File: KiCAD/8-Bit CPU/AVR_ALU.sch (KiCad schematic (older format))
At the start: 23 parts, among them J2 AVRISP, U20 74HC377, U21 ATmega16-16AU, U22 74HC245, U23 74HC173

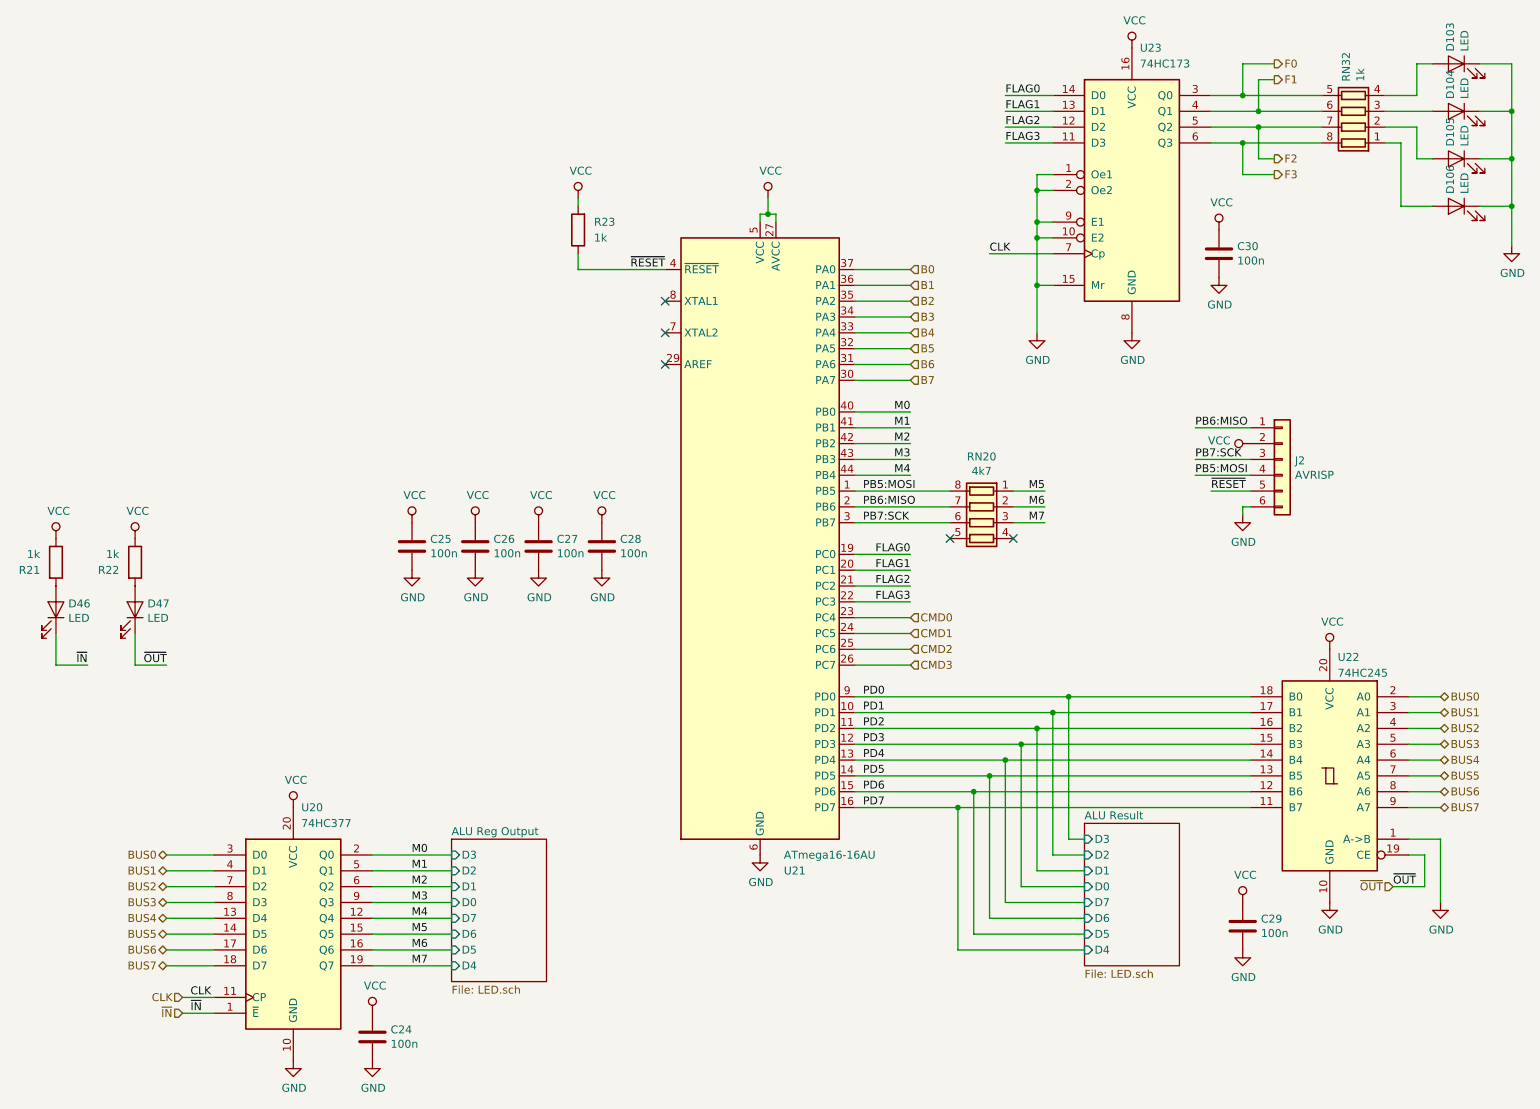
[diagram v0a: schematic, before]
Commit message: KiCAD cleanup - Revision A
Revision A Known Issues:
 * ATTiny45 has incorrect footprint
 * Flags register is redundant (The ATMega16's output port is a register)
 * Power jack pinout is wrong (12V shorted to ground)
 * Step counter reset logic is wrong (Active high signalling, Active low input)
 * ALU output indicator not connected
 * HLT indicator missing
 * EEPROMs can't be page written due to addressing setup (minor annoyance)
 * Flags Logic uses NAND gates instead of AND (fixed on the board I built)
 * Programmer needs to be able to toggle EEPROM outputs and Addressing Devices
    with different signals to enable reading.
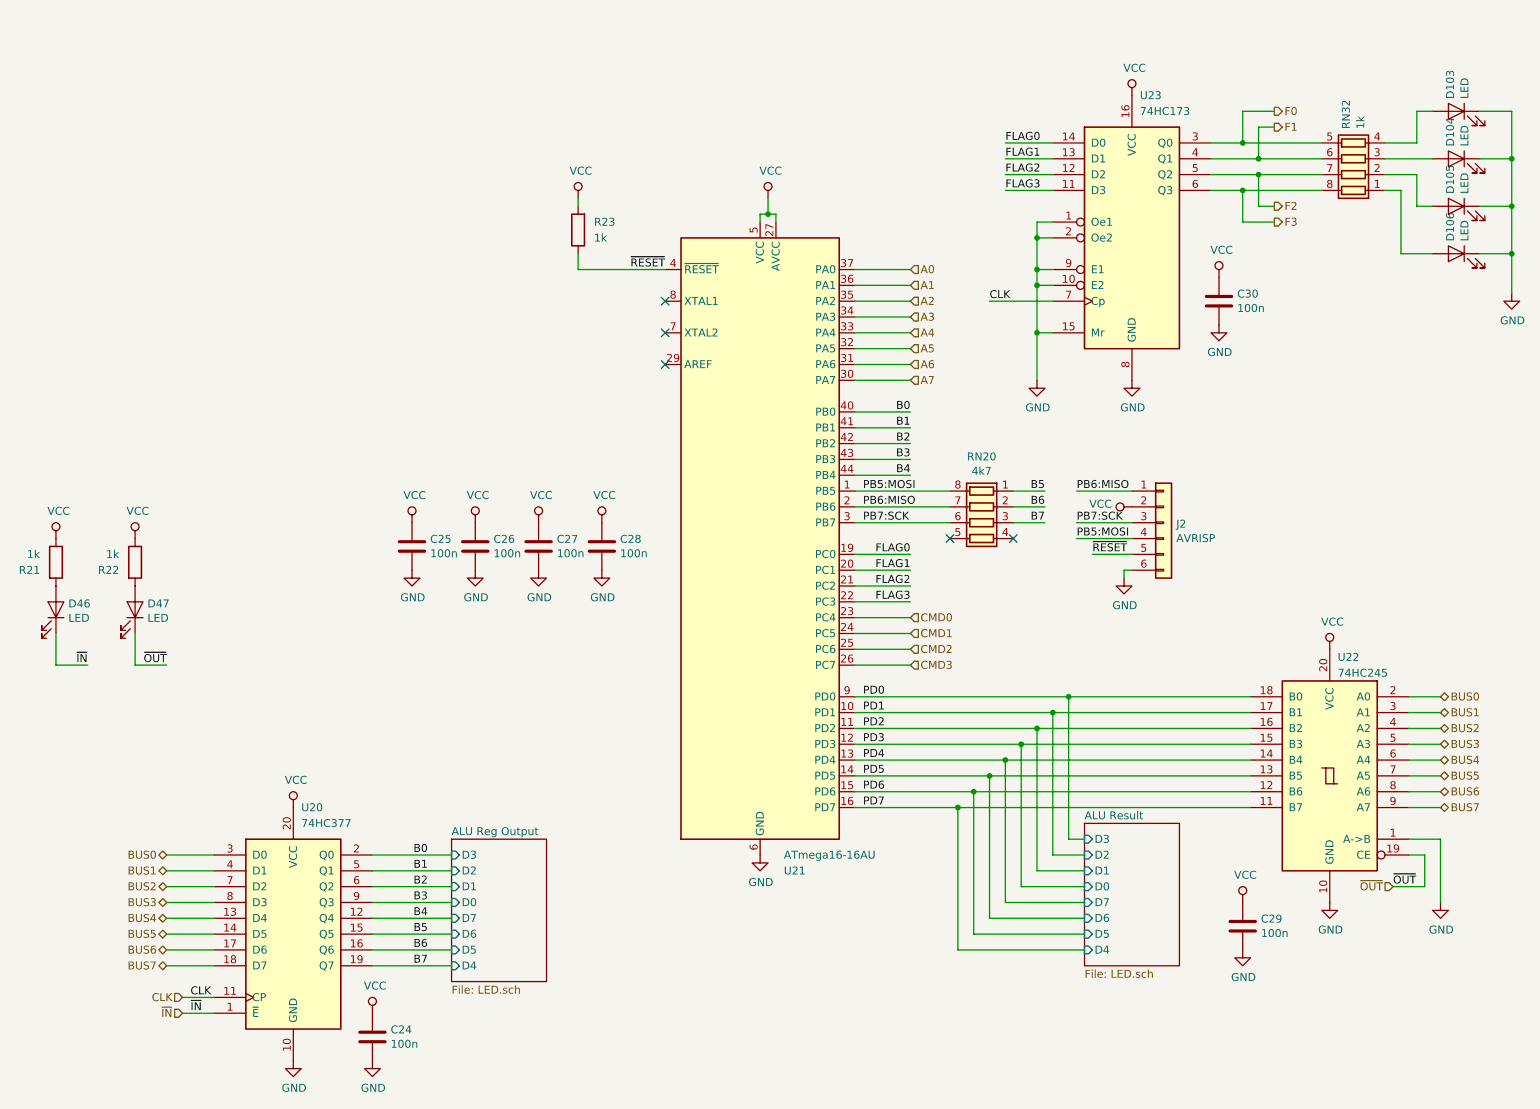
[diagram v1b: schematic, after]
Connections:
- net M0 is gone; now on net B0: U20.2 (Q0), U21.40 (PB0)
- net M1 is gone; now on net B1: U20.5 (Q1), U21.41 (PB1)
- net M2 is gone; now on net B2: U20.6 (Q2), U21.42 (PB2)
- net M3 is gone; now on net B3: U20.9 (Q3), U21.43 (PB3)
- net M4 is gone; now on net B4: U20.12 (Q4), U21.44 (PB4)
- net M5 is gone; now on net B5: RN20.1 (R1.1), U20.15 (Q5)
- net M6 is gone; now on net B6: RN20.2 (R2.1), U20.16 (Q6)
- net M7 is gone; now on net B7: RN20.3 (R3.1), U20.19 (Q7)
- net B0: no longer U21.37 (PA0)
- net B1: no longer U21.36 (PA1)
- net B2: no longer U21.35 (PA2)
- net B3: no longer U21.34 (PA3)
- net B4: no longer U21.33 (PA4)
- net B5: no longer U21.32 (PA5)
- net B6: no longer U21.31 (PA6)
- net B7: no longer U21.30 (PA7)
- new net A0: U21.37 (PA0)
- new net A1: U21.36 (PA1)
- new net A2: U21.35 (PA2)
- new net A3: U21.34 (PA3)
- new net A4: U21.33 (PA4)
- new net A5: U21.32 (PA5)
- new net A6: U21.31 (PA6)
- new net A7: U21.30 (PA7)
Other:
- moved on the sheet: C30, D103, D104, D105, D106, J2, RN32, U23

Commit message: KiCAD files update & Gerbers
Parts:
- removed C30: 100n, Capacitor_SMD:C_0805_2012Metric, symbol Device:C
- removed R23: 1k, Resistor_SMD:R_0805_2012Metric, symbol Device:R
- removed U23: 74HC173, jcf:SOIC-16_3.9x9.9mm_P1.27mm_JCF, symbol 74xx:74LS173
- renumbered C25 to C24, C26 to C25, C27 to C26, C28 to C27, C29 to C28, C24 to C29, D103 to D46, D104 to D47, D105 to D48, D106 to D49, D46 to D50, D47 to D51, RN32 to RN21, U21 to U20, U22 to U21, U20 to U22
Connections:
- net FLAG0 is gone; now on net F0: U20.19 (PC0)
- net FLAG1 is gone; now on net F1: U20.20 (PC1)
- net FLAG2 is gone; now on net F2: U20.21 (PC2)
- net FLAG3 is gone; now on net F3: U20.22 (PC3)
- net F0: now also RN21.8 (R1.2); no longer RN21.5 (R4.2)
- net F1: now also RN21.7 (R2.2); no longer RN21.6 (R3.2)
- net F2: now also RN21.6 (R3.2); no longer RN21.7 (R2.2)
- net F3: now also RN21.5 (R4.2); no longer RN21.8 (R1.2)
- net VCC: now also RN20.4 (R4.1)
- net ~RESET: now also RN20.5 (R4.2)
- net at RN21.1 (R1.1): now also D46.2 (A); no longer D49.2 (A)
- net at RN21.2 (R2.1): now also D47.2 (A); no longer D48.2 (A)
- net at RN21.3 (R3.1): now also D48.2 (A); no longer D47.2 (A)
- net at RN21.4 (R4.1): now also D49.2 (A); no longer D46.2 (A)
- no-connect marks 5 -> 3
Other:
- moved on the sheet: D46, D47, D48, D49, J2, RN20, RN21
